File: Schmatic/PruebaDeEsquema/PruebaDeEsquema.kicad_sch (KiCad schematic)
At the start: 48 parts, among them J2 Conn_01x02_Pin, U3 TLV1117-33, U4 TLV4888, U5 TLV4888, U6 TLV1117-ADJ

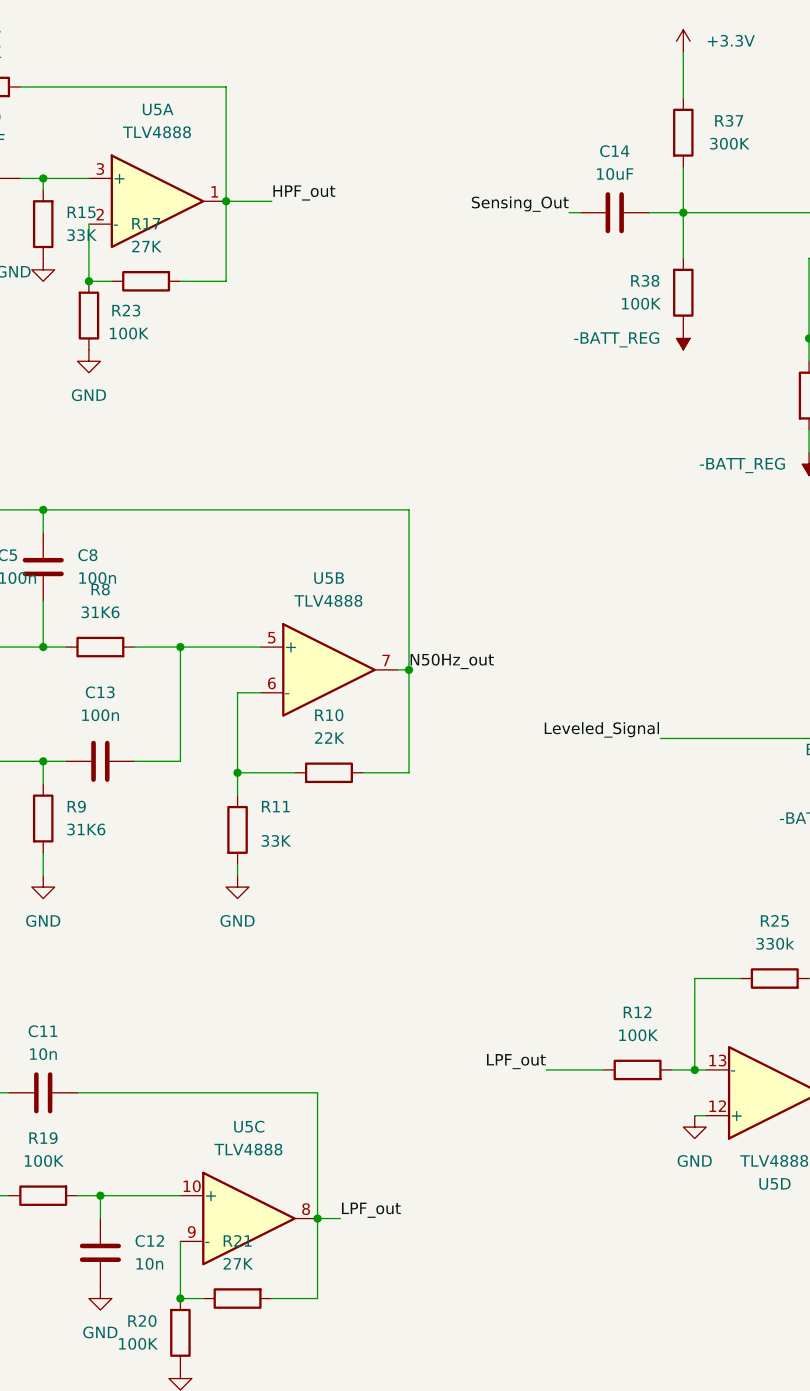
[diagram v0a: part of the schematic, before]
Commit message: Stabilize ECG filter stage outputs
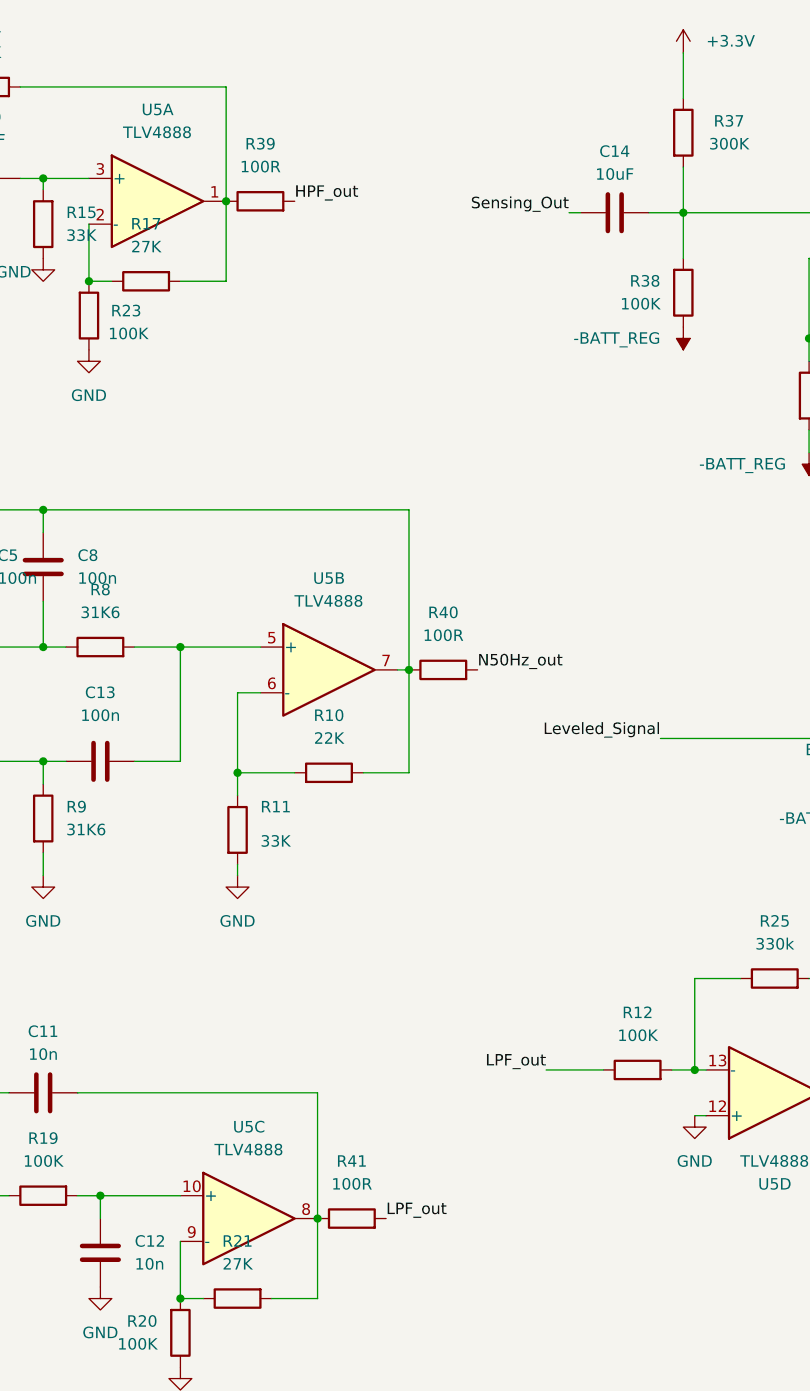
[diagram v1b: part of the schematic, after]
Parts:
- added R39, R40, R41: 100R, Resistor_SMD:R_0805_2012Metric_Pad1.20x1.40mm_HandSolder, symbol Device:R
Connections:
- net HPF_out: now also R39.2; no longer R14.2, R17.2, U5.1
- net LPF_out: now also R41.2; no longer C11.2, R21.2, U5.8
- net N50Hz_out: now also R40.2; no longer C5.1, C8.1, R10.2, U5.7
- new net: C11.2, R21.2, R41.1, U5.8
- new net: C5.1, C8.1, R10.2, R40.1, U5.7
- new net: R14.2, R17.2, R39.1, U5.1
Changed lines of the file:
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@@
 	(wire
 		(pts
-			(xy 101.6 52.07) (xy 106.68 52.07)
-		)
-		(stroke
-			(width 0)
-			(type default)
-		)
-	)
-	(wire
-		(pts
 			(xy 96.52 60.96) (xy 101.6 60.96)
 		)
@@
 	(wire
 		(pts
-			(xy 111.76 165.1) (xy 114.3 165.1)
-		)
-		(stroke
-			(width 0)
-			(type default)
-		)
-	)
-	(wire
-		(pts
 			(xy 121.92 104.14) (xy 120.65 104.14)
 		)
@@
 	)
 	(label "N50Hz_out"
-		(at 121.92 104.14 0)
+		(at 129.54 104.14 0)
 		(effects
 			(font
@@
 	)
 	(label "LPF_out"
-		(at 114.3 165.1 0)
+		(at 119.38 165.1 0)
 		(effects
 			(font
@@
 	)
 	(label "HPF_out"
-		(at 106.68 52.07 0)
+		(at 109.22 52.07 0)
 		(effects
 			(font
@@
 		)
 	)
+	(symbol
+		(lib_name "R_6")
+		(lib_id "Device:R")
+		(at 105.41 52.07 90)
+		(unit 1)
+		(body_style 1)
+		(exclude_from_sim no)
+		(in_bom yes)
+		(on_board yes)
+		(in_pos_files yes)
+		(dnp no)
+		(fields_autoplaced yes)
+		(property "Reference" "R39"
+			(at 105.41 45.72 90)
+			(show_name no)
+			(do_not_autoplace no)
+			(effects
+				(font
+					(size 1.27 1.27)
+				)
+			)
+		)
+		(property "Value" "100R"
+			(at 105.41 48.26 90)
+			(show_name no)
+			(do_not_autoplace no)
+			(effects
+				(font
+					(size 1.27 1.27)
+				)
+			)
+		)
+		(property "Footprint" "Resistor_SMD:R_0805_2012Metric_Pad1.20x1.40mm_HandSolder" (at 105.41 53.848 90) (hide yes) (show_name no) (do_not_autoplace no) (effects (font (size 1.27 1.27))))
+		(property "Datasheet" "" (at 105.41 52.07 0) (hide yes) (show_name no) (do_not_autoplace no) (effects (font (size 1.27 1.27))))
+		(property "Description" "Resistencia serie de aislamiento para estabilizar la salida del operacional entre etapas sin mover la frecuencia de corte" (at 105.41 52.07 0) (hide yes) (show_name no) (do_not_autoplace no) (effects (font (size 1.27 1.27))))
+		(pin "1")
+		(pin "2")
+		(instances (project "PruebaDeEsquema" (path "/f6a3e494-1c0c-4c12-b53f-ef642a44780c" (reference "R39") (unit 1))))
+	)
+	(symbol
+		(lib_name "R_6")
+		(lib_id "Device:R")
+		(at 125.73 104.14 90)
+		(unit 1)
+		(body_style 1)
+		(exclude_from_sim no)
+		(in_bom yes)
+		(on_board yes)
+		(in_pos_files yes)
+		(dnp no)
+		(fields_autoplaced yes)
+		(property "Reference" "R40"
+			(at 125.73 97.79 90)
+			(show_name no)
+			(do_not_autoplace no)
+			(effects
+				(font
+					(size 1.27 1.27)
+				)
+			)
+		)
+		(property "Value" "100R"
+			(at 125.73 100.33 90)
+			(show_name no)
+			(do_not_autoplace no)
+			(effects
+				(font
+					(size 1.27 1.27)
+				)
+			)
+		)
+		(property "Footprint" "Resistor_SMD:R_0805_2012Metric_Pad1.20x1.40mm_HandSolder" (at 125.73 105.918 90) (hide yes) (show_name no) (do_not_autoplace no) (effects (font (size 1.27 1.27))))
+		(property "Datasheet" "" (at 125.73 104.14 0) (hide yes) (show_name no) (do_not_autoplace no) (effects (font (size 1.27 1.27))))
+		(property "Description" "Resistencia serie de aislamiento para estabilizar la salida del operacional entre etapas sin mover la frecuencia de corte" (at 125.73 104.14 0) (hide yes) (show_name no) (do_not_autoplace no) (effects (font (size 1.27 1.27))))
+		(pin "1")
+		(pin "2")
+		(instances (project "PruebaDeEsquema" (path "/f6a3e494-1c0c-4c12-b53f-ef642a44780c" (reference "R40") (unit 1))))
+	)
+	(symbol
+		(lib_name "R_6")
+		(lib_id "Device:R")
+		(at 115.57 165.1 90)
+		(unit 1)
+		(body_style 1)
+		(exclude_from_sim no)
+		(in_bom yes)
+		(on_board yes)
+		(in_pos_files yes)
+		(dnp no)
+		(fields_autoplaced yes)
+		(property "Reference" "R41"
+			(at 115.57 158.75 90)
+			(show_name no)
+			(do_not_autoplace no)
+			(effects
+				(font
+					(size 1.27 1.27)
+				)
+			)
+		)
+		(property "Value" "100R"
+			(at 115.57 161.29 90)
+			(show_name no)
+			(do_not_autoplace no)
+			(effects
+				(font
+					(size 1.27 1.27)
+				)
+			)
+		)
+		(property "Footprint" "Resistor_SMD:R_0805_2012Metric_Pad1.20x1.40mm_HandSolder" (at 115.57 166.878 90) (hide yes) (show_name no) (do_not_autoplace no) (effects (font (size 1.27 1.27))))
+		(property "Datasheet" "" (at 115.57 165.1 0) (hide yes) (show_name no) (do_not_autoplace no) (effects (font (size 1.27 1.27))))
+		(property "Description" "Resistencia serie de aislamiento para estabilizar la salida del operacional entre etapas sin mover la frecuencia de corte" (at 115.57 165.1 0) (hide yes) (show_name no) (do_not_autoplace no) (effects (font (size 1.27 1.27))))
+		(pin "1")
+		(pin "2")
+		(instances (project "PruebaDeEsquema" (path "/f6a3e494-1c0c-4c12-b53f-ef642a44780c" (reference "R41") (unit 1))))
+	)
 	(sheet_instances
